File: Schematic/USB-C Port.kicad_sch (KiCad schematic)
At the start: 9 parts, among them J10 USB_C_Receptacle_USB2.0_14P, U6 TVS2200DRV

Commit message: added sensors?
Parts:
- added C44, C45: 4u7, symbol Device:C
- C46: renamed from C43; value 4u7 -> 100n
- renumbered C42 to C47, C41 to C48, C40 to C49, C39 to C50, FB5 to FB9, J10 to J8
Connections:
- net GND: now also C44.1, C45.1
- net VBUS: now also C44.2, C45.2
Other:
- moved on the sheet: C46

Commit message: 1st Schematic Review
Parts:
- renumbered C44 to C47, C45 to C48, C46 to C49, C47 to C50, C48 to C51, C49 to C52, C50 to C53, U6 to U9
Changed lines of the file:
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@@
 		(on_board yes)
 		(dnp no)
-		(property "Reference" "C48"
+		(property "Reference" "C51"
 			(at 161.29 70.104 90)
 			(effects
@@
 			(project "STAR"
 				(path "/fc8533bc-25dd-4c20-9b4c-ffebebd6739b/ec72a35b-e7f2-4422-8859-60e9fb848154/f6f5f8c2-3fe5-486c-93b1-10011acff681"
-					(reference "C48")
+					(reference "C51")
 					(unit 1)
 				)
@@
 		(on_board yes)
 		(dnp no)
-		(property "Reference" "C49"
+		(property "Reference" "C52"
 			(at 161.29 75.184 90)
 			(effects
@@
 			(project "STAR"
 				(path "/fc8533bc-25dd-4c20-9b4c-ffebebd6739b/ec72a35b-e7f2-4422-8859-60e9fb848154/f6f5f8c2-3fe5-486c-93b1-10011acff681"
-					(reference "C49")
+					(reference "C52")
 					(unit 1)
 				)
@@
 		(on_board yes)
 		(dnp no)
-		(property "Reference" "#PWR037"
+		(property "Reference" "#PWR042"
 			(at 110.49 142.24 0)
 			(effects
@@
 			(project "STAR"
 				(path "/fc8533bc-25dd-4c20-9b4c-ffebebd6739b/ec72a35b-e7f2-4422-8859-60e9fb848154/f6f5f8c2-3fe5-486c-93b1-10011acff681"
-					(reference "#PWR037")
+					(reference "#PWR042")
 					(unit 1)
 				)
@@
 		(on_board yes)
 		(dnp no)
-		(property "Reference" "C45"
+		(property "Reference" "C48"
 			(at 127 73.914 90)
 			(effects
@@
 			(project "STAR"
 				(path "/fc8533bc-25dd-4c20-9b4c-ffebebd6739b/ec72a35b-e7f2-4422-8859-60e9fb848154/f6f5f8c2-3fe5-486c-93b1-10011acff681"
-					(reference "C45")
+					(reference "C48")
 					(unit 1)
 				)
@@
 		(on_board yes)
 		(dnp no)
-		(property "Reference" "#PWR039"
+		(property "Reference" "#PWR044"
 			(at 176.53 120.65 0)
 			(effects
@@
 			(project "STAR"
 				(path "/fc8533bc-25dd-4c20-9b4c-ffebebd6739b/ec72a35b-e7f2-4422-8859-60e9fb848154/f6f5f8c2-3fe5-486c-93b1-10011acff681"
-					(reference "#PWR039")
+					(reference "#PWR044")
 					(unit 1)
 				)
@@
 		(dnp no)
 		(fields_autoplaced yes)
-		(property "Reference" "U6"
+		(property "Reference" "U9"
 			(at 162.56 86.36 90)
 			(effects
@@
 			(project ""
 				(path "/fc8533bc-25dd-4c20-9b4c-ffebebd6739b/ec72a35b-e7f2-4422-8859-60e9fb848154/f6f5f8c2-3fe5-486c-93b1-10011acff681"
-					(reference "U6")
+					(reference "U9")
 					(unit 1)
 				)
@@
 		(on_board yes)
 		(dnp no)
-		(property "Reference" "C44"
+		(property "Reference" "C47"
 			(at 127 68.834 90)
 			(effects
@@
 			(project "STAR"
 				(path "/fc8533bc-25dd-4c20-9b4c-ffebebd6739b/ec72a35b-e7f2-4422-8859-60e9fb848154/f6f5f8c2-3fe5-486c-93b1-10011acff681"
-					(reference "C44")
+					(reference "C47")
 					(unit 1)
 				)
@@
 		(on_board yes)
 		(dnp no)
-		(property "Reference" "C50"
+		(property "Reference" "C53"
 			(at 161.29 80.264 90)
 			(effects
@@
 			(project "STAR"
 				(path "/fc8533bc-25dd-4c20-9b4c-ffebebd6739b/ec72a35b-e7f2-4422-8859-60e9fb848154/f6f5f8c2-3fe5-486c-93b1-10011acff681"
-					(reference "C50")
+					(reference "C53")
 					(unit 1)
 				)
@@
 		(on_board yes)
 		(dnp no)
-		(property "Reference" "C47"
+		(property "Reference" "C50"
 			(at 161.29 65.024 90)
 			(effects
@@
 			(project "STAR"
 				(path "/fc8533bc-25dd-4c20-9b4c-ffebebd6739b/ec72a35b-e7f2-4422-8859-60e9fb848154/f6f5f8c2-3fe5-486c-93b1-10011acff681"
-					(reference "C47")
+					(reference "C50")
 					(unit 1)
 				)
@@
 		(on_board yes)
 		(dnp no)
-		(property "Reference" "C46"
+		(property "Reference" "C49"
 			(at 127 78.994 90)
 			(effects
@@
 			(project "STAR"
 				(path "/fc8533bc-25dd-4c20-9b4c-ffebebd6739b/ec72a35b-e7f2-4422-8859-60e9fb848154/f6f5f8c2-3fe5-486c-93b1-10011acff681"
-					(reference "C46")
+					(reference "C49")
 					(unit 1)
 				)
@@
 		(on_board yes)
 		(dnp no)
-		(property "Reference" "#PWR038"
+		(property "Reference" "#PWR043"
 			(at 123.19 87.63 0)
 			(effects
@@
 			(project "STAR"
 				(path "/fc8533bc-25dd-4c20-9b4c-ffebebd6739b/ec72a35b-e7f2-4422-8859-60e9fb848154/f6f5f8c2-3fe5-486c-93b1-10011acff681"
-					(reference "#PWR038")
+					(reference "#PWR043")
 					(unit 1)
 				)

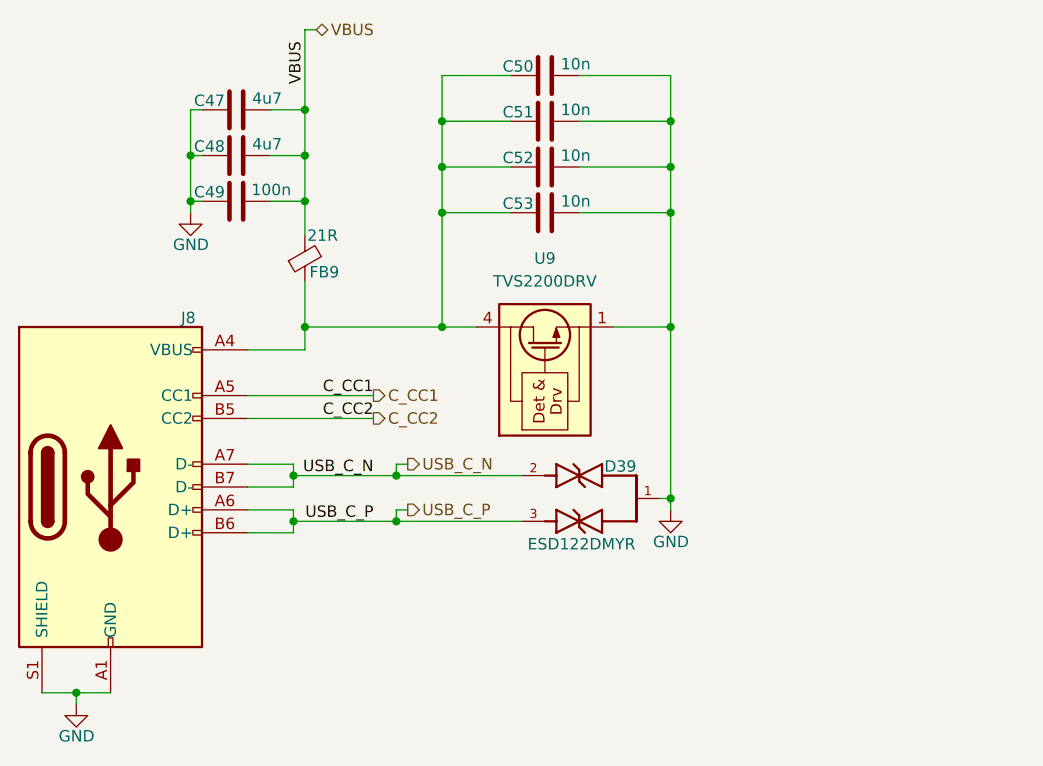
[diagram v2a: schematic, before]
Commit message: added so many test points
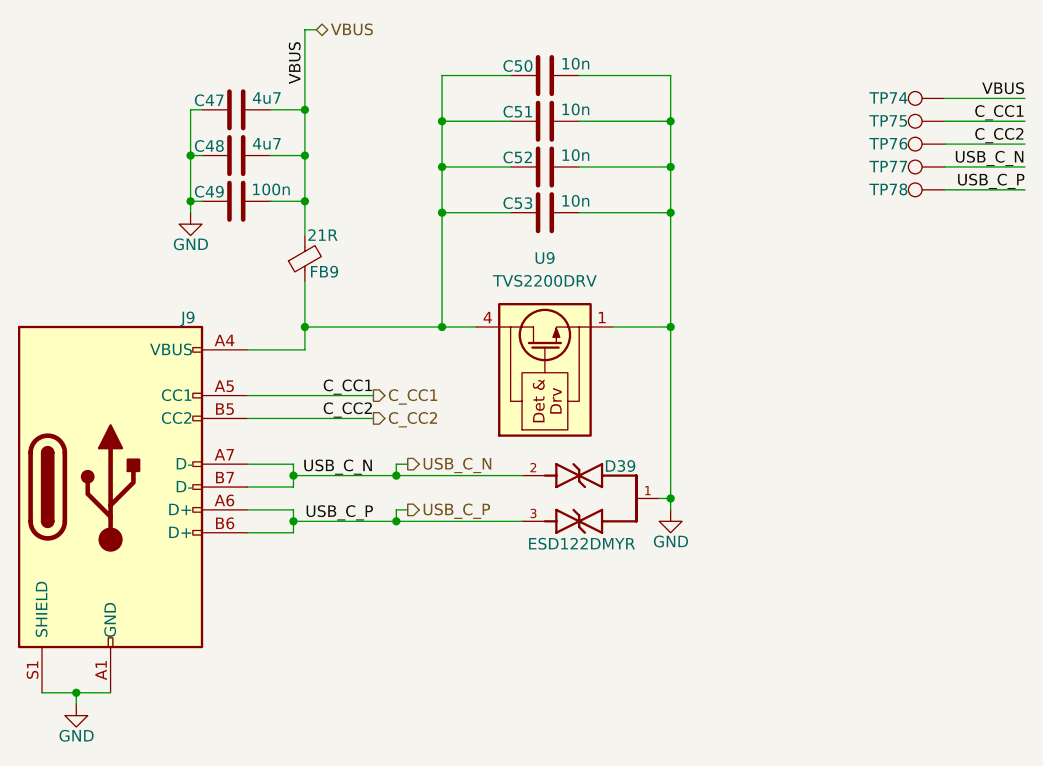
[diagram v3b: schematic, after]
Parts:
- added TP74, TP75, TP76, TP77, TP78: TestPoint, symbol Connector:TestPoint
- renumbered J8 to J9
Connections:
- net C_CC1: now also TP75.1
- net C_CC2: now also TP76.1
- net USB_C_N: now also TP77.1
- net USB_C_P: now also TP78.1
- net VBUS: now also TP74.1

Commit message: updates
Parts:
- renumbered D39 to D41
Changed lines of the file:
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@@
 		(on_board yes)
 		(dnp no)
-		(property "Reference" "D39"
+		(property "Reference" "D41"
 			(at 170.942 109.474 0)
 			(effects
@@
 			(project ""
 				(path "/fc8533bc-25dd-4c20-9b4c-ffebebd6739b/ec72a35b-e7f2-4422-8859-60e9fb848154/f6f5f8c2-3fe5-486c-93b1-10011acff681"
-					(reference "D39")
+					(reference "D41")
 					(unit 1)
 				)

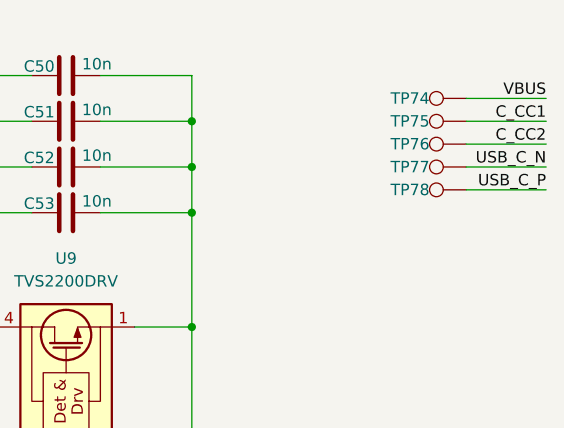
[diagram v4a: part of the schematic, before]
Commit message: updated fuel guage
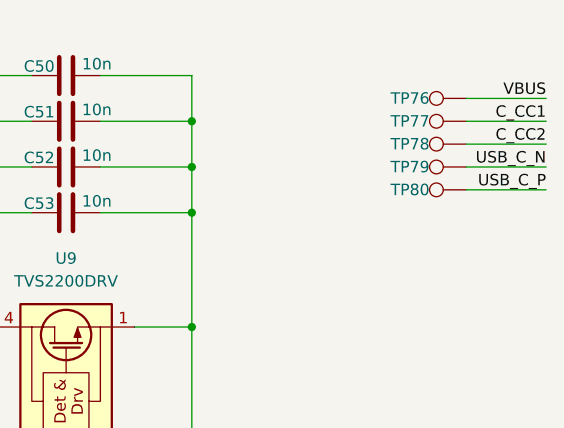
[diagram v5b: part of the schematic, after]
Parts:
- renumbered TP74 to TP76, TP75 to TP77, TP76 to TP78, TP77 to TP79, TP78 to TP80
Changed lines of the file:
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@@
 		(on_board yes)
 		(dnp no)
-		(property "Reference" "TP78"
+		(property "Reference" "TP80"
 			(at 202.946 78.74 90)
 			(effects
@@
 			(project "STAR"
 				(path "/fc8533bc-25dd-4c20-9b4c-ffebebd6739b/ec72a35b-e7f2-4422-8859-60e9fb848154/f6f5f8c2-3fe5-486c-93b1-10011acff681"
-					(reference "TP78")
+					(reference "TP80")
 					(unit 1)
 				)
@@
 		(on_board yes)
 		(dnp no)
-		(property "Reference" "TP74"
+		(property "Reference" "TP76"
 			(at 202.946 68.58 90)
 			(effects
@@
 			(project "STAR"
 				(path "/fc8533bc-25dd-4c20-9b4c-ffebebd6739b/ec72a35b-e7f2-4422-8859-60e9fb848154/f6f5f8c2-3fe5-486c-93b1-10011acff681"
-					(reference "TP74")
+					(reference "TP76")
 					(unit 1)
 				)
@@
 		(on_board yes)
 		(dnp no)
-		(property "Reference" "TP75"
+		(property "Reference" "TP77"
 			(at 202.946 71.12 90)
 			(effects
@@
 			(project "STAR"
 				(path "/fc8533bc-25dd-4c20-9b4c-ffebebd6739b/ec72a35b-e7f2-4422-8859-60e9fb848154/f6f5f8c2-3fe5-486c-93b1-10011acff681"
-					(reference "TP75")
+					(reference "TP77")
 					(unit 1)
 				)
@@
 		(on_board yes)
 		(dnp no)
-		(property "Reference" "TP76"
+		(property "Reference" "TP78"
 			(at 202.946 73.66 90)
 			(effects
@@
 			(project "STAR"
 				(path "/fc8533bc-25dd-4c20-9b4c-ffebebd6739b/ec72a35b-e7f2-4422-8859-60e9fb848154/f6f5f8c2-3fe5-486c-93b1-10011acff681"
-					(reference "TP76")
+					(reference "TP78")
 					(unit 1)
 				)
@@
 		(on_board yes)
 		(dnp no)
-		(property "Reference" "TP77"
+		(property "Reference" "TP79"
 			(at 202.946 76.2 90)
 			(effects
@@
 			(project "STAR"
 				(path "/fc8533bc-25dd-4c20-9b4c-ffebebd6739b/ec72a35b-e7f2-4422-8859-60e9fb848154/f6f5f8c2-3fe5-486c-93b1-10011acff681"
-					(reference "TP77")
+					(reference "TP79")
 					(unit 1)
 				)

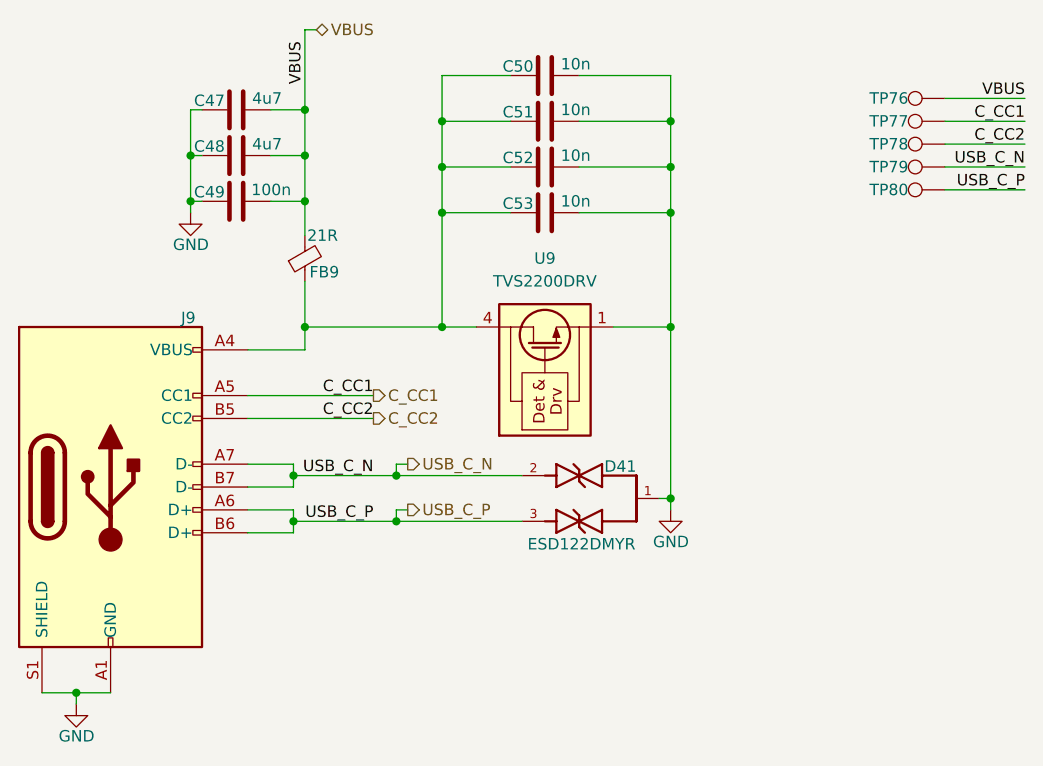
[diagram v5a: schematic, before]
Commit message: Added MCU
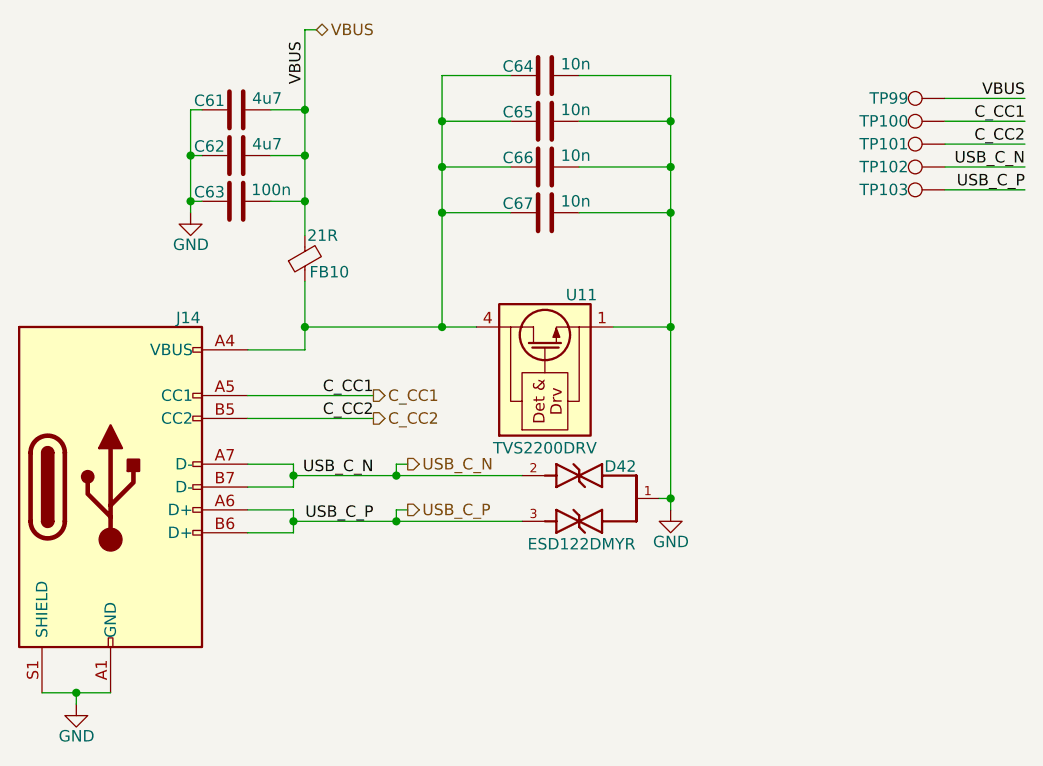
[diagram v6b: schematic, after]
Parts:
- renumbered C47 to C61, C48 to C62, C49 to C63, C50 to C64, C51 to C65, C52 to C66, C53 to C67, D41 to D42, FB9 to FB10, J9 to J14, TP77 to TP100, TP78 to TP101, TP79 to TP102, TP80 to TP103, TP76 to TP99, U9 to U11
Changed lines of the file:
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@@
 		(on_board yes)
 		(dnp no)
-		(property "Reference" "C51"
+		(property "Reference" "C65"
 			(at 161.29 70.104 90)
 			(effects
@@
 			(project "STAR"
 				(path "/fc8533bc-25dd-4c20-9b4c-ffebebd6739b/ec72a35b-e7f2-4422-8859-60e9fb848154/f6f5f8c2-3fe5-486c-93b1-10011acff681"
-					(reference "C51")
+					(reference "C65")
 					(unit 1)
 				)
@@
 		(on_board yes)
 		(dnp no)
-		(property "Reference" "C52"
+		(property "Reference" "C66"
 			(at 161.29 75.184 90)
 			(effects
@@
 			(project "STAR"
 				(path "/fc8533bc-25dd-4c20-9b4c-ffebebd6739b/ec72a35b-e7f2-4422-8859-60e9fb848154/f6f5f8c2-3fe5-486c-93b1-10011acff681"
-					(reference "C52")
+					(reference "C66")
 					(unit 1)
 				)
@@
 		(on_board yes)
 		(dnp no)
-		(property "Reference" "#PWR043"
+		(property "Reference" "#PWR052"
 			(at 110.49 142.24 0)
 			(effects
@@
 			(project "STAR"
 				(path "/fc8533bc-25dd-4c20-9b4c-ffebebd6739b/ec72a35b-e7f2-4422-8859-60e9fb848154/f6f5f8c2-3fe5-486c-93b1-10011acff681"
-					(reference "#PWR043")
+					(reference "#PWR052")
 					(unit 1)
 				)
@@
 		(on_board yes)
 		(dnp no)
-		(property "Reference" "C48"
+		(property "Reference" "C62"
 			(at 127 73.914 90)
 			(effects
@@
 			(project "STAR"
 				(path "/fc8533bc-25dd-4c20-9b4c-ffebebd6739b/ec72a35b-e7f2-4422-8859-60e9fb848154/f6f5f8c2-3fe5-486c-93b1-10011acff681"
-					(reference "C48")
+					(reference "C62")
 					(unit 1)
 				)
@@
 		(on_board yes)
 		(dnp no)
-		(property "Reference" "FB9"
+		(property "Reference" "FB10"
 			(at 136.398 87.884 0)
 			(effects
@@
 			(project "STAR"
 				(path "/fc8533bc-25dd-4c20-9b4c-ffebebd6739b/ec72a35b-e7f2-4422-8859-60e9fb848154/f6f5f8c2-3fe5-486c-93b1-10011acff681"
-					(reference "FB9")
+					(reference "FB10")
 					(unit 1)
 				)
@@
 		(on_board yes)
 		(dnp no)
-		(property "Reference" "#PWR045"
+		(property "Reference" "#PWR054"
 			(at 176.53 120.65 0)
 			(effects
@@
 			(project "STAR"
 				(path "/fc8533bc-25dd-4c20-9b4c-ffebebd6739b/ec72a35b-e7f2-4422-8859-60e9fb848154/f6f5f8c2-3fe5-486c-93b1-10011acff681"
-					(reference "#PWR045")
+					(reference "#PWR054")
 					(unit 1)
 				)
@@
 		(on_board yes)
 		(dnp no)
-		(fields_autoplaced yes)
-		(property "Reference" "U9"
-			(at 162.56 86.36 90)
+		(property "Reference" "U11"
+			(at 166.624 90.424 90)
 			(effects
 				(font
@@
 		)
 		(property "Value" "TVS2200DRV"
-			(at 162.56 88.9 90)
+			(at 162.56 107.442 90)
 			(effects
 				(font
@@
 			(project ""
 				(path "/fc8533bc-25dd-4c20-9b4c-ffebebd6739b/ec72a35b-e7f2-4422-8859-60e9fb848154/f6f5f8c2-3fe5-486c-93b1-10011acff681"
-					(reference "U9")
+					(reference "U11")
 					(unit 1)
 				)
@@
 		(on_board yes)
 		(dnp no)
-		(property "Reference" "C47"
+		(property "Reference" "C61"
 			(at 127 68.834 90)
 			(effects
@@
 			(project "STAR"
 				(path "/fc8533bc-25dd-4c20-9b4c-ffebebd6739b/ec72a35b-e7f2-4422-8859-60e9fb848154/f6f5f8c2-3fe5-486c-93b1-10011acff681"
-					(reference "C47")
+					(reference "C61")
 					(unit 1)
 				)
@@
 		(on_board yes)
 		(dnp no)
-		(property "Reference" "J9"
+		(property "Reference" "J14"
 			(at 122.936 92.964 0)
 			(effects
@@
 			(project ""
 				(path "/fc8533bc-25dd-4c20-9b4c-ffebebd6739b/ec72a35b-e7f2-4422-8859-60e9fb848154/f6f5f8c2-3fe5-486c-93b1-10011acff681"
-					(reference "J9")
+					(reference "J14")
 					(unit 1)
 				)
@@
 		(on_board yes)
 		(dnp no)
-		(property "Reference" "TP80"
+		(property "Reference" "TP103"
 			(at 202.946 78.74 90)
 			(effects
@@
 			(project "STAR"
 				(path "/fc8533bc-25dd-4c20-9b4c-ffebebd6739b/ec72a35b-e7f2-4422-8859-60e9fb848154/f6f5f8c2-3fe5-486c-93b1-10011acff681"
-					(reference "TP80")
+					(reference "TP103")
 					(unit 1)
 				)
@@
 		(on_board yes)
 		(dnp no)
-		(property "Reference" "C53"
+		(property "Reference" "C67"
 			(at 161.29 80.264 90)
 			(effects
@@
 			(project "STAR"
 				(path "/fc8533bc-25dd-4c20-9b4c-ffebebd6739b/ec72a35b-e7f2-4422-8859-60e9fb848154/f6f5f8c2-3fe5-486c-93b1-10011acff681"
-					(reference "C53")
+					(reference "C67")
 					(unit 1)
 				)
@@
 		(on_board yes)
 		(dnp no)
-		(property "Reference" "D41"
+		(property "Reference" "D42"
 			(at 170.942 109.474 0)
 			(effects
@@
 			(project ""
 				(path "/fc8533bc-25dd-4c20-9b4c-ffebebd6739b/ec72a35b-e7f2-4422-8859-60e9fb848154/f6f5f8c2-3fe5-486c-93b1-10011acff681"
-					(reference "D41")
+					(reference "D42")
 					(unit 1)
 				)
@@
 		(on_board yes)
 		(dnp no)
-		(property "Reference" "TP76"
+		(property "Reference" "TP99"
 			(at 202.946 68.58 90)
 			(effects
@@
 			(project "STAR"
 				(path "/fc8533bc-25dd-4c20-9b4c-ffebebd6739b/ec72a35b-e7f2-4422-8859-60e9fb848154/f6f5f8c2-3fe5-486c-93b1-10011acff681"
-					(reference "TP76")
+					(reference "TP99")
 					(unit 1)
 				)
@@
 		(on_board yes)
 		(dnp no)
-		(property "Reference" "C50"
+		(property "Reference" "C64"
 			(at 161.29 65.024 90)
 			(effects
@@
 			(project "STAR"
 				(path "/fc8533bc-25dd-4c20-9b4c-ffebebd6739b/ec72a35b-e7f2-4422-8859-60e9fb848154/f6f5f8c2-3fe5-486c-93b1-10011acff681"
-					(reference "C50")
+					(reference "C64")
 					(unit 1)
 				)
@@
 		(on_board yes)
 		(dnp no)
-		(property "Reference" "TP77"
+		(property "Reference" "TP100"
 			(at 202.946 71.12 90)
 			(effects
@@
 			(project "STAR"
 				(path "/fc8533bc-25dd-4c20-9b4c-ffebebd6739b/ec72a35b-e7f2-4422-8859-60e9fb848154/f6f5f8c2-3fe5-486c-93b1-10011acff681"
-					(reference "TP77")
+					(reference "TP100")
 					(unit 1)
 				)
@@
 		(on_board yes)
 		(dnp no)
-		(property "Reference" "TP78"
+		(property "Reference" "TP101"
 			(at 202.946 73.66 90)
 			(effects
@@
 			(project "STAR"
 				(path "/fc8533bc-25dd-4c20-9b4c-ffebebd6739b/ec72a35b-e7f2-4422-8859-60e9fb848154/f6f5f8c2-3fe5-486c-93b1-10011acff681"
-					(reference "TP78")
+					(reference "TP101")
 					(unit 1)
 				)
@@
 		(on_board yes)
 		(dnp no)
-		(property "Reference" "C49"
+		(property "Reference" "C63"
 			(at 127 78.994 90)
 			(effects
@@
 			(project "STAR"
 				(path "/fc8533bc-25dd-4c20-9b4c-ffebebd6739b/ec72a35b-e7f2-4422-8859-60e9fb848154/f6f5f8c2-3fe5-486c-93b1-10011acff681"
-					(reference "C49")
+					(reference "C63")
 					(unit 1)
 				)
@@
 		(on_board yes)
 		(dnp no)
-		(property "Reference" "#PWR044"
+		(property "Reference" "#PWR053"
 			(at 123.19 87.63 0)
 			(effects
@@
 			(project "STAR"
 				(path "/fc8533bc-25dd-4c20-9b4c-ffebebd6739b/ec72a35b-e7f2-4422-8859-60e9fb848154/f6f5f8c2-3fe5-486c-93b1-10011acff681"
-					(reference "#PWR044")
+					(reference "#PWR053")
 					(unit 1)
 				)
@@
 		(on_board yes)
 		(dnp no)
-		(property "Reference" "TP79"
+		(property "Reference" "TP102"
 			(at 202.946 76.2 90)
 			(effects
@@
 			(project "STAR"
 				(path "/fc8533bc-25dd-4c20-9b4c-ffebebd6739b/ec72a35b-e7f2-4422-8859-60e9fb848154/f6f5f8c2-3fe5-486c-93b1-10011acff681"
-					(reference "TP79")
+					(reference "TP102")
 					(unit 1)
 				)
